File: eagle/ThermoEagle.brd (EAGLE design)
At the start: 100 x 80 mm, 35 parts, among them IC1 MAX232, IC2 4511N, Q1 20MHz, T1 2N2219, T2 2N2219, U1 LM324

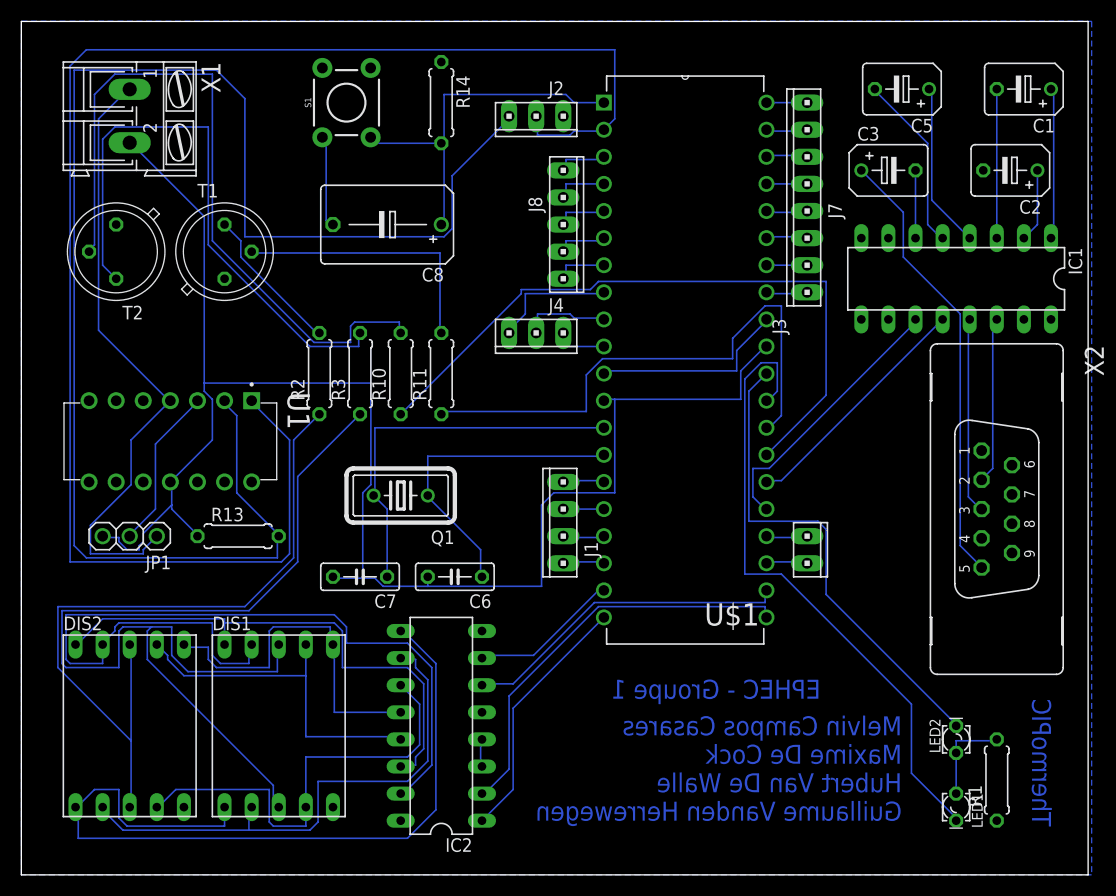
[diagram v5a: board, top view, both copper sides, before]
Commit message: Update Eagle files (schema + board)
I hope this time it's the final update.
- Added GND and VCC labels for componenets Maxime had forgotten,
- Updated board with new routes, etc.
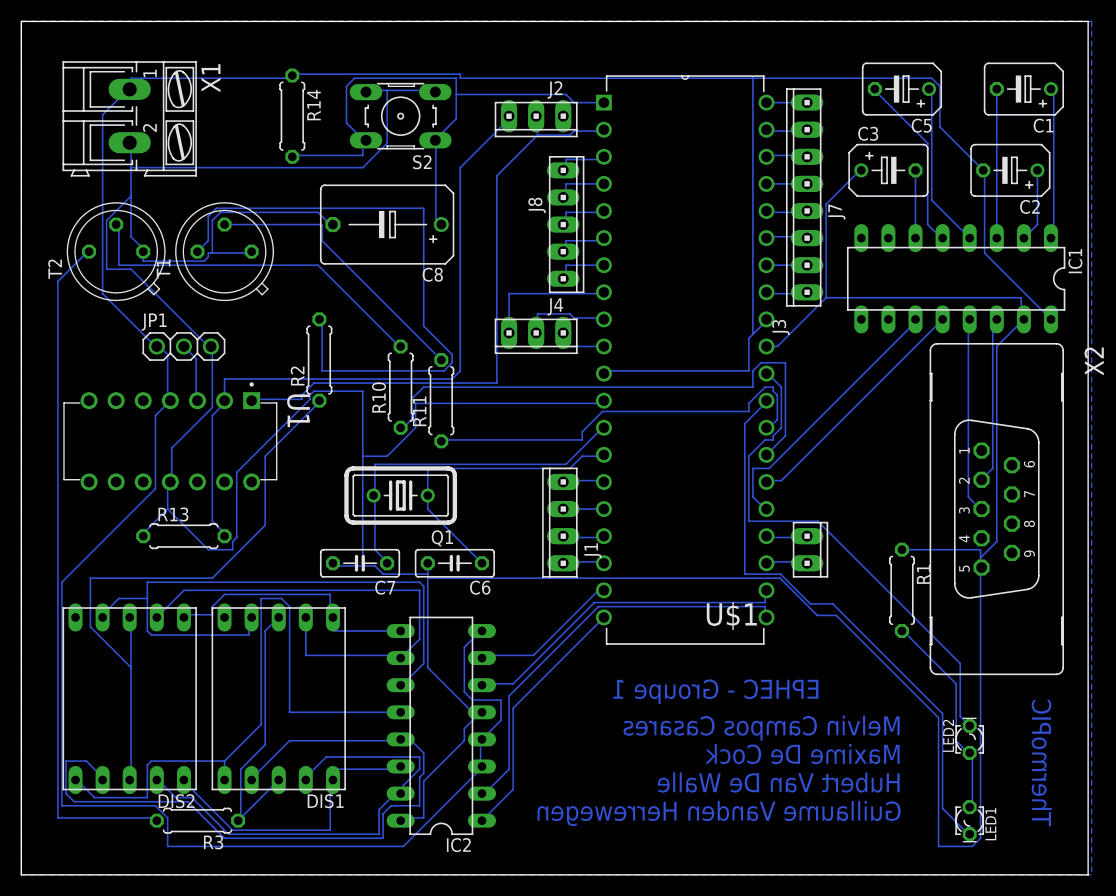
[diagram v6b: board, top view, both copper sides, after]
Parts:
- removed S1: MOMENTARY-SWITCH-SPST-PTH-6.0MM, SparkFun-Switches:TACTILE_SWITCH_PTH_6.0MM
- added S2: (no value), DC_LOAD_AU:B3F-10XX
- moved R3 44.6 mm to (16.5, 5.08), turned to 180 degrees
- moved R1 19.9 mm to (82.5, 26.7), turned to 270 degrees
- moved JP1 18.5 mm to (15.2, 49.5), turned to 0 degrees
- moved R14 14.0 mm to (25.4, 71.1)
- moved R13 5.08 mm to (15.2, 31.8)
- moved DIS1 2.54 mm to (24.1, 16.5), turned to 180 degrees
- moved DIS2 2.54 mm to (10.2, 16.5), turned to 180 degrees
- moved R11 2.54 mm to (39.4, 44.5)
- moved LED1 1.80 mm to (88.9, 5.08)
- moved LED2 1.27 mm to (88.9, 12.7)
- moved R10 1.27 mm to (35.6, 45.7)
- moved C6 1.27 mm to (40.6, 29.2)
- moved C7 1.27 mm to (31.8, 29.2)
- moved R2 1.27 mm to (27.9, 48.3)
- turned T1 to 90 degrees
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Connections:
- removed net N$18: C2.-
- removed net N$20: C3.+, X2.5
- removed net N$29: T1.1
- removed net N$39: IC1.16
- removed net N$40: IC1.15
- removed net N$42: IC2.8
- removed net N$43: IC2.16
- removed net N$46: R1.1
- removed net N$55: IC2.5
- removed net N$56: C8.-, S1.1
- removed net N$57: R14.1
- removed net N$73: IC2.3, IC2.4
- removed net N$8: T2.1
- net GND: now also C3.+, C8.-, IC1.15, IC2.16, IC2.5, R1.1, S2.3, S2.4, T1.1, T2.1, X2.5
- net N$72: now also S2.1, S2.2; no longer S1.3
- net VCC: now also C2.-, IC1.16, IC2.3, IC2.4, IC2.8, R14.1
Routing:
- net GND: track 150.1 -> 398.2 mm
- net VCC: track 76.4 -> 285.4 mm
- net N$49: track 151.0 -> 57.0 mm
- net N$31: track 143.5 -> 63.9 mm
- net N$7: track 97.2 -> 25.7 mm
- net N$24: track 75.3 -> 25.0 mm
- net N$9: track 14.1 -> 57.3 mm
- net N$20: track 41.9 -> 0.00 mm
- net N$10: track 80.1 -> 43.9 mm
- net N$28: track 33.1 -> 68.2 mm
- net N$4: track 66.6 -> 33.6 mm
- net N$27: track 33.4 -> 59.6 mm
- net N$36: track 49.8 -> 28.0 mm
- net N$72: track 35.2 -> 53.7 mm
- net N$26: track 41.8 -> 57.4 mm
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
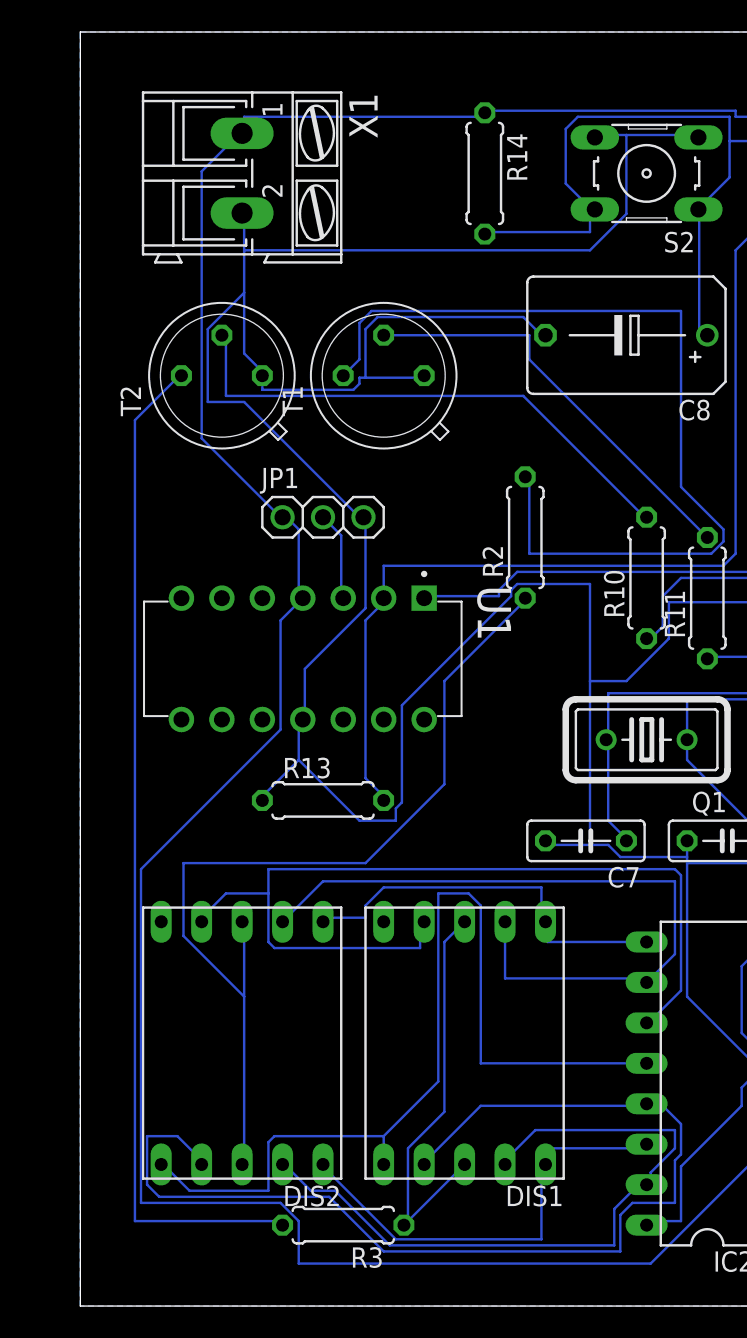
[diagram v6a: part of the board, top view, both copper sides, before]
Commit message: Update board... idk
Moved the alimentation port in a right place and in the right
orientation.
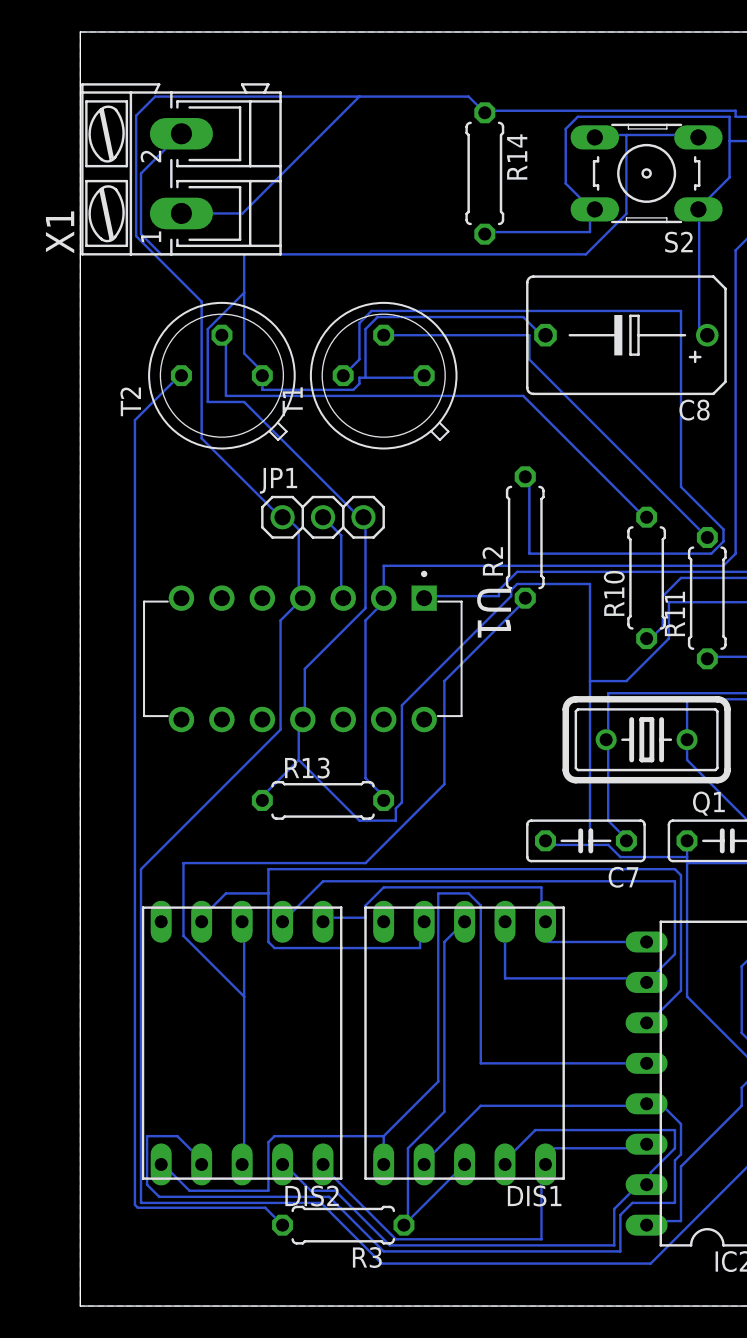
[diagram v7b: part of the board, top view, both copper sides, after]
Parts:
- moved X1 3.81 mm to (6.35, 71.1), turned to 90 degrees
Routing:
- net VCC: track 285.4 -> 306.3 mm
- net GND: track 398.2 -> 410.0 mm
- net N$30: track 63.8 -> 63.1 mm
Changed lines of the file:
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@@
 <layer number="21" name="tPlace" color="7" fill="1" visible="yes" active="yes"/>
 <layer number="22" name="bPlace" color="7" fill="1" visible="no" active="yes"/>
-<layer number="23" name="tOrigins" color="15" fill="1" visible="yes" active="yes"/>
+<layer number="23" name="tOrigins" color="15" fill="1" visible="no" active="yes"/>
 <layer number="24" name="bOrigins" color="15" fill="1" visible="no" active="yes"/>
 <layer number="25" name="tNames" color="7" fill="1" visible="no" active="yes"/>
@@
 <attribute name="VALUE" x="1.3831" y="45.01921875" size="2.086009375" layer="27" ratio="10" rot="SR270"/>
 </element>
-<element name="X1" library="con-ptr500" library_urn="urn:adsk.eagle:library:181" package="AK300/2" package3d_urn="urn:adsk.eagle:package:9881/1" value="" x="10.16" y="71.12" smashed="yes" rot="R270">
-<attribute name="MF" value="" x="-57.15" y="19.05" size="1.778" layer="27" rot="R270" display="off"/>
-<attribute name="MPN" value="" x="-57.15" y="19.05" size="1.778" layer="27" rot="R270" display="off"/>
-<attribute name="NAME" x="16.891" y="76.2" size="1.778" layer="25" ratio="10" rot="R270"/>
-<attribute name="OC_FARNELL" value="unknown" x="-57.15" y="19.05" size="1.778" layer="27" rot="R270" display="off"/>
-<attribute name="OC_NEWARK" value="unknown" x="-57.15" y="19.05" size="1.778" layer="27" rot="R270" display="off"/>
-<attribute name="VALUE" x="1.524" y="76.2" size="1.778" layer="27" ratio="10" rot="R270"/>
+<element name="X1" library="con-ptr500" library_urn="urn:adsk.eagle:library:181" package="AK300/2" package3d_urn="urn:adsk.eagle:package:9881/1" value="" x="6.35" y="71.12" smashed="yes" rot="R90">
+<attribute name="MF" value="" x="73.66" y="123.19" size="1.778" layer="27" rot="R90" display="off"/>
+<attribute name="MPN" value="" x="73.66" y="123.19" size="1.778" layer="27" rot="R90" display="off"/>
+<attribute name="NAME" x="-0.381" y="66.04" size="1.778" layer="25" ratio="10" rot="R90"/>
+<attribute name="OC_FARNELL" value="unknown" x="73.66" y="123.19" size="1.778" layer="27" rot="R90" display="off"/>
+<attribute name="OC_NEWARK" value="unknown" x="73.66" y="123.19" size="1.778" layer="27" rot="R90" display="off"/>
+<attribute name="VALUE" x="14.986" y="66.04" size="1.778" layer="27" ratio="10" rot="R90"/>
 </element>
 <element name="X2" library="con-subd" library_urn="urn:adsk.eagle:library:189" package="F09VB" package3d_urn="urn:adsk.eagle:package:10282/1" value="" x="91.44" y="34.29" smashed="yes" rot="R270">
@@
 <wire x1="12.954" y1="49.53" x2="12.7" y2="49.53" width="0.1524" layer="16"/>
 <wire x1="13.716" y1="44.577" x2="13.97" y2="44.45" width="0.1524" layer="16"/>
-<wire x1="10.287" y1="74.676" x2="25.146" y2="74.676" width="0.1524" layer="16"/>
-<wire x1="10.287" y1="73.914" x2="10.287" y2="74.676" width="0.1524" layer="16"/>
-<wire x1="25.146" y1="74.676" x2="25.4" y2="74.93" width="0.1524" layer="16"/>
-<wire x1="10.287" y1="73.914" x2="10.16" y2="73.6346" width="0.1524" layer="16"/>
-<wire x1="7.62" y1="54.483" x2="12.573" y2="49.53" width="0.1524" layer="16"/>
-<wire x1="7.62" y1="71.247" x2="7.62" y2="54.483" width="0.1524" layer="16"/>
-<wire x1="9.906" y1="73.533" x2="7.62" y2="71.247" width="0.1524" layer="16"/>
+<wire x1="25.4" y1="74.93" x2="24.384" y2="75.946" width="0.1524" layer="16"/>
+<wire x1="24.384" y1="75.946" x2="17.526" y2="75.946" width="0.1524" layer="16"/>
+<wire x1="12.573" y1="49.53" x2="7.62" y2="54.483" width="0.1524" layer="16"/>
 <wire x1="12.573" y1="49.53" x2="12.7" y2="49.53" width="0.1524" layer="16"/>
-<wire x1="9.906" y1="73.533" x2="10.16" y2="73.6346" width="0.1524" layer="16"/>
 <wire x1="35.814" y1="2.667" x2="43.053" y2="9.906" width="0.1524" layer="16"/>
-<wire x1="13.716" y1="2.667" x2="35.814" y2="2.667" width="0.1524" layer="16"/>
-<wire x1="13.716" y1="5.334" x2="13.716" y2="2.667" width="0.1524" layer="16"/>
-<wire x1="12.573" y1="6.477" x2="13.716" y2="5.334" width="0.1524" layer="16"/>
-<wire x1="3.81" y1="6.477" x2="12.573" y2="6.477" width="0.1524" layer="16"/>
+<wire x1="18.923" y1="2.667" x2="35.814" y2="2.667" width="0.1524" layer="16"/>
+<wire x1="15.113" y1="6.477" x2="18.923" y2="2.667" width="0.1524" layer="16"/>
+<wire x1="3.81" y1="6.477" x2="15.113" y2="6.477" width="0.1524" layer="16"/>
 <wire x1="3.81" y1="27.432" x2="3.81" y2="6.477" width="0.1524" layer="16"/>
 <wire x1="12.573" y1="36.195" x2="3.81" y2="27.432" width="0.1524" layer="16"/>
@@
 <wire x1="25.527" y1="75.057" x2="41.148" y2="75.057" width="0.1524" layer="16"/>
 <wire x1="25.527" y1="75.057" x2="25.4" y2="74.93" width="0.1524" layer="16"/>
+<wire x1="17.526" y1="75.946" x2="10.16" y2="68.58" width="0.1524" layer="16"/>
+<wire x1="10.16" y1="68.58" x2="10.1346" y2="68.6054" width="0.1524" layer="16"/>
+<wire x1="10.1346" y1="68.6054" x2="6.35" y2="68.6054" width="0.1524" layer="16"/>
+<wire x1="4.7019875" y1="75.946" x2="17.526" y2="75.946" width="0.1524" layer="16"/>
+<wire x1="3.5052" y1="67.18374375" x2="3.5052" y2="74.7492125" width="0.1524" layer="16"/>
+<wire x1="3.5052" y1="74.7492125" x2="4.7019875" y2="75.946" width="0.1524" layer="16"/>
+<wire x1="7.62" y1="54.483" x2="7.62" y2="63.06894375" width="0.1524" layer="16"/>
+<wire x1="7.62" y1="63.06894375" x2="3.5052" y2="67.18374375" width="0.1524" layer="16"/>
 </signal>
 <signal name="GND">
@@
 <wire x1="38.481" y1="73.533" x2="38.8112" y2="73.3806" width="0.1524" layer="16"/>
 <wire x1="10.287" y1="59.817" x2="11.43" y2="58.674" width="0.1524" layer="16"/>
-<wire x1="10.287" y1="68.58" x2="10.287" y2="66.294" width="0.1524" layer="16"/>
-<wire x1="10.287" y1="66.294" x2="10.287" y2="63.627" width="0.1524" layer="16"/>
+<wire x1="10.287" y1="66.04" x2="10.287" y2="63.627" width="0.1524" layer="16"/>
 <wire x1="10.287" y1="63.627" x2="10.287" y2="59.817" width="0.1524" layer="16"/>
 <wire x1="11.43" y1="58.674" x2="11.43" y2="58.42" width="0.1524" layer="16"/>
-<wire x1="10.287" y1="68.58" x2="10.16" y2="68.6308" width="0.1524" layer="16"/>
 <wire x1="17.526" y1="58.293" x2="17.907" y2="58.293" width="0.1524" layer="16"/>
 <wire x1="17.907" y1="58.293" x2="21.336" y2="58.293" width="0.1524" layer="16"/>
@@
 <wire x1="28.956" y1="60.96" x2="29.21" y2="60.96" width="0.1524" layer="16"/>
 <wire x1="34.29" y1="68.58" x2="34.29" y2="73.533" width="0.1524" layer="16"/>
-<wire x1="32.004" y1="66.294" x2="34.29" y2="68.58" width="0.1524" layer="16"/>
-<wire x1="10.287" y1="66.294" x2="32.004" y2="66.294" width="0.1524" layer="16"/>
+<wire x1="31.75" y1="66.04" x2="34.29" y2="68.58" width="0.1524" layer="16"/>
+<wire x1="10.287" y1="66.04" x2="31.75" y2="66.04" width="0.1524" layer="16"/>
 <wire x1="10.287" y1="56.769" x2="17.526" y2="49.53" width="0.1524" layer="16"/>
 <wire x1="8.001" y1="56.769" x2="10.287" y2="56.769" width="0.1524" layer="16"/>
@@
 <vertex x="0" y="0"/>
 </polygon>
+<wire x1="6.3246" y1="73.6346" x2="6.35" y2="73.6092" width="0.1524" layer="16"/>
+<wire x1="5.08" y1="66.04" x2="10.287" y2="66.04" width="0.1524" layer="16"/>
+<wire x1="3.81" y1="67.31" x2="3.81" y2="71.12" width="0.1524" layer="16"/>
+<wire x1="3.81" y1="67.31" x2="5.08" y2="66.04" width="0.1524" layer="16"/>
+<wire x1="3.81" y1="71.12" x2="6.3246" y2="73.6346" width="0.1524" layer="16"/>
 </signal>
 <signal name="N$2">
@@
 <contactref element="R3" pad="2"/>
 <contactref element="T2" pad="3"/>
-<wire x1="3.429" y1="5.334" x2="12.573" y2="5.334" width="0.1524" layer="16"/>
-<wire x1="3.429" y1="55.626" x2="3.429" y2="5.334" width="0.1524" layer="16"/>
+<wire x1="3.429" y1="55.626" x2="3.429" y2="6.35" width="0.1524" layer="16"/>
 <wire x1="6.096" y1="58.293" x2="3.429" y2="55.626" width="0.1524" layer="16"/>
-<wire x1="12.573" y1="5.334" x2="12.7" y2="5.08" width="0.1524" layer="16"/>
 <wire x1="6.096" y1="58.293" x2="6.35" y2="58.42" width="0.1524" layer="16"/>
+<wire x1="3.429" y1="6.35" x2="3.6068" y2="6.1722" width="0.1524" layer="16"/>
+<wire x1="11.6078" y1="6.1722" x2="12.7" y2="5.08" width="0.1524" layer="16"/>
+<wire x1="3.6068" y1="6.1722" x2="11.6078" y2="6.1722" width="0.1524" layer="16"/>
 </signal>
 <signal name="N$31">

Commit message: Update Board - validation #2 by EuroCircuit
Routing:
- net GND: track 410.0 -> 0.00 mm
- net N$38: track 50.0 -> 183.2 mm
- net N$27: track 59.6 -> 188.9 mm
- net N$70: track 3.89 -> 74.2 mm
- net N$4: track 33.6 -> 82.8 mm
- net N$9: track 57.3 -> 14.3 mm
- net VCC: track 306.3 -> 341.2 mm
- net N$37: track 47.7 -> 63.1 mm
- net N$25: track 45.4 -> 32.4 mm
- net N$31: track 63.9 -> 76.7 mm
- net N$6: track 23.8 -> 36.2 mm
- net RX: track 22.8 -> 31.3 mm
- net N$72: track 53.7 -> 45.7 mm
- net N$28: track 68.2 -> 60.6 mm
- net N$1: track 14.1 -> 19.6 mm
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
